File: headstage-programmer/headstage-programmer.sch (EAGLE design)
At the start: 26 parts, among them Q1 DMP3056L, U1 TPS61202

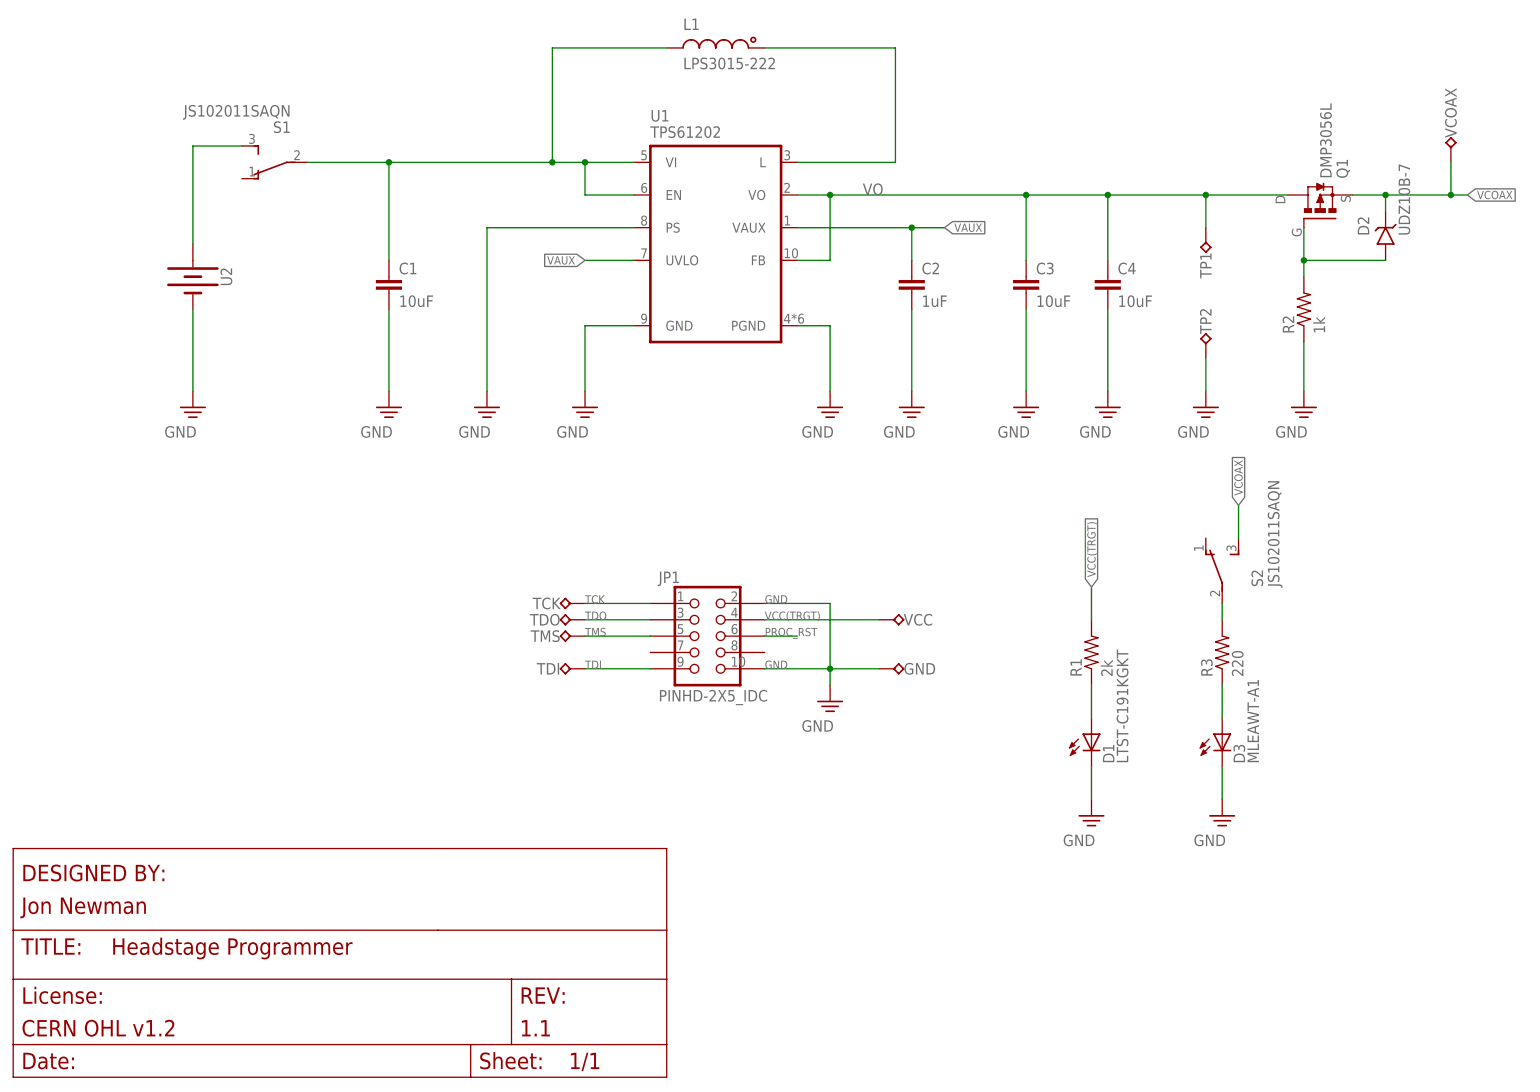
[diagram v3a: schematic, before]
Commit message: Update headstage programmer with side mout switch
- I hacked this into the previous revision because it makes programming
much easier since you have control over system power after making sure
pins are aligned. This updates the board to have this funcationality
wihtout the hack
- Got rid of bottom side LED -- cute idea, but did nothing in practice.
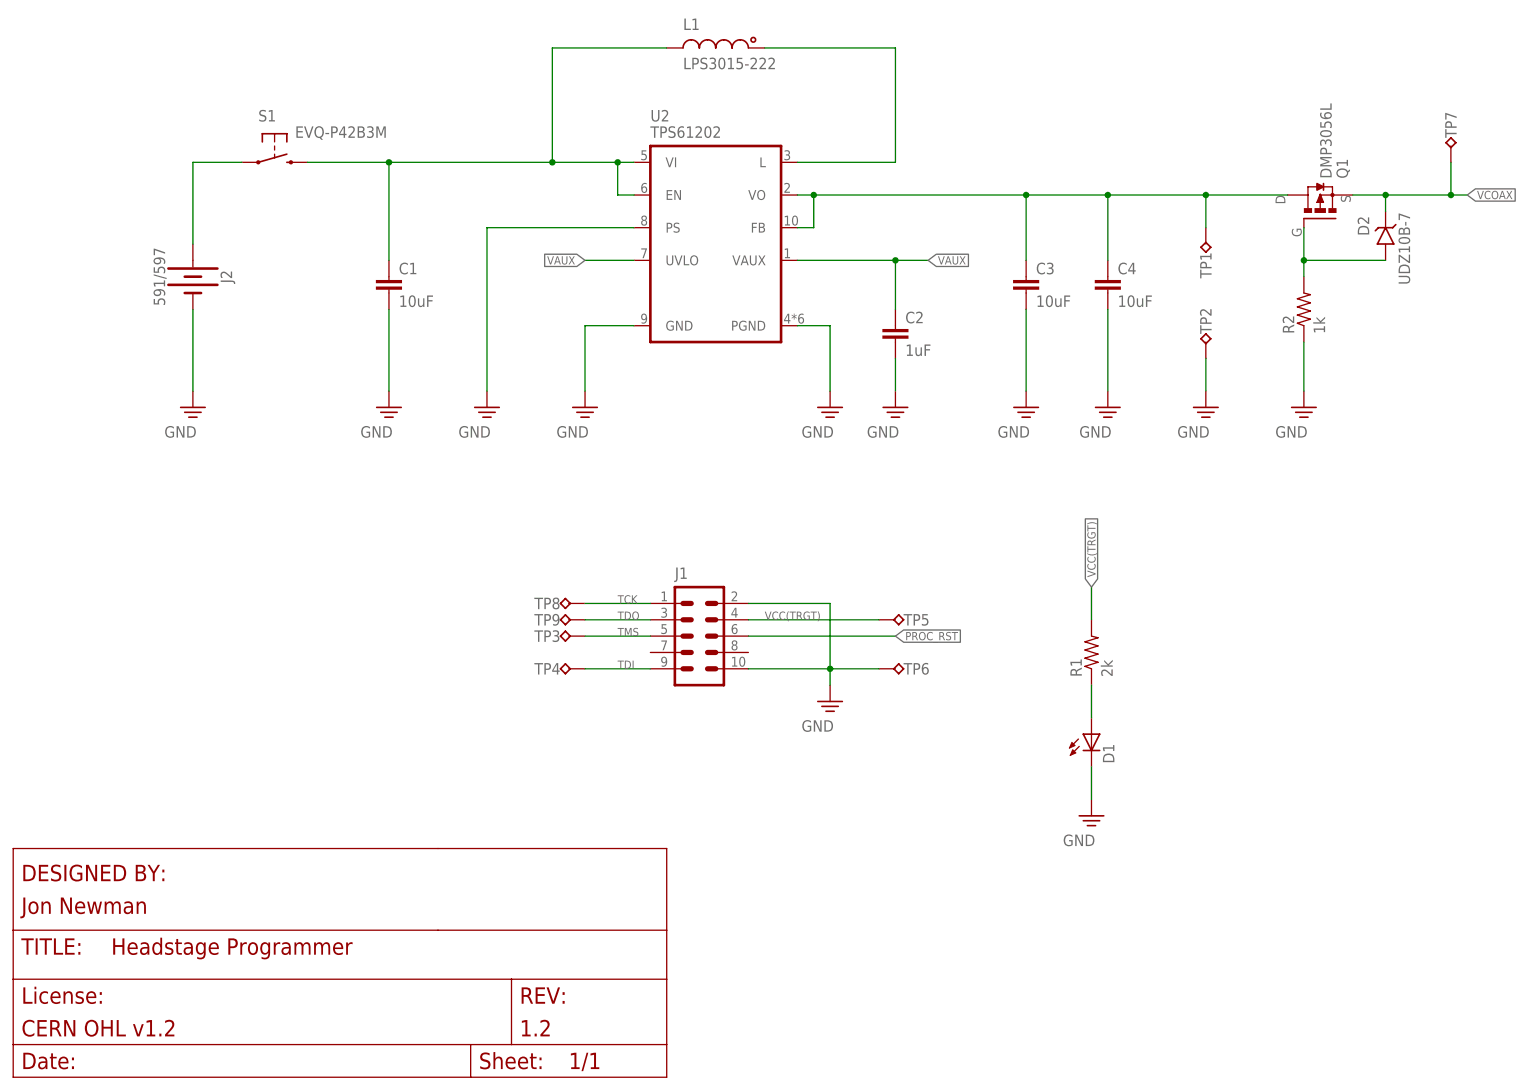
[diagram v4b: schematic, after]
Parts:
- removed D3: MLEAWT-A1, jonnew:LED_MLE-HS-CAT
- removed JP1: PINHD-2X5_IDC, jonnew:PINHD-2X5_IDC
- removed R3: 220, jonnew:R_0805
- removed S2: JS102011SAQN, jonnew:SPDT_JS
- removed U1: TPS61202, jonnew:TPS61200
- added J1: 302-S101, jonnew:PINHD-2X5_IDC
- added J2: 591/597, jonnew:BATTERY_597/591
- D1: value LTST-C191KGKT -> (none)
- S1: value JS102011SAQN -> EVQ-P42B3M; device jonnew:SPDT_JS -> jonnew:SPST_TACT2_EVQP4
- U2: value (none) -> TPS61202; device jonnew:BATTERY_597/591 -> jonnew:TPS61200
- renumbered GND to TP6, TCK to TP8, TDI to TP4, TDO to TP9, TMS to TP3, VCC to TP5, VCOAX to TP7
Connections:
- removed net N$2: D3.A, R3.1
- removed net N$6: R3.2, S2.2
- net GND: now also J1.10, J1.2, J2.-, U2.GND, U2.PGND, U2.PS; no longer D3.C, JP1.10, JP1.2, U1.GND, U1.PGND, U1.PS, U2.-
- net N$3: now also U2.L; no longer U1.L
- net N$4: now also J2.+, S1.P; no longer S1.3, U2.+
- net PROC_RST: now also J1.6; no longer JP1.6
- net TCK: now also J1.1; no longer JP1.1
- net TDI: now also J1.9; no longer JP1.9
- net TDO: now also J1.3; no longer JP1.3
- net TMS: now also J1.5; no longer JP1.5
- net VAUX: now also U2.UVLO, U2.VAUX; no longer U1.UVLO, U1.VAUX
- net VCC(TRGT): now also J1.4; no longer JP1.4
- net VCOAX: no longer S2.3
- net VIN: now also S1.S, U2.EN, U2.VI; no longer S1.2, U1.EN, U1.VI
- net VO: now also U2.FB, U2.VO; no longer U1.FB, U1.VO
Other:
- moved on the sheet: C2
